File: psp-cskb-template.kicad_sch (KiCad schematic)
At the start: 6 parts, among them J1 Conn_02x26_Odd_Even, J2 Conn_02x26_Odd_Even

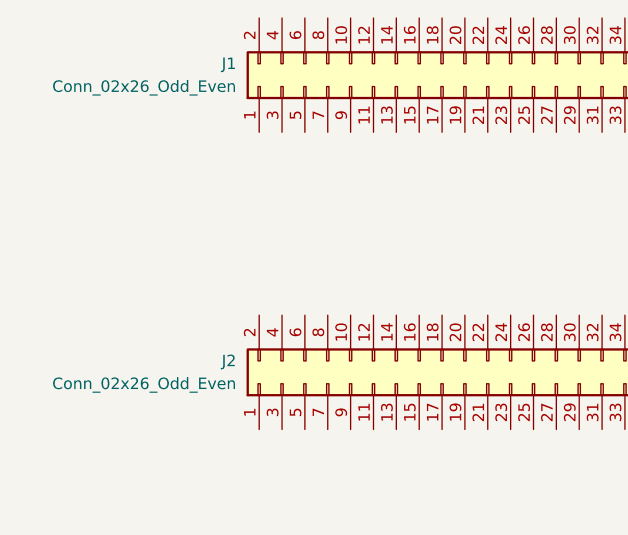
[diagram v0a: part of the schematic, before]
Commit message: flip CSKB header numbers
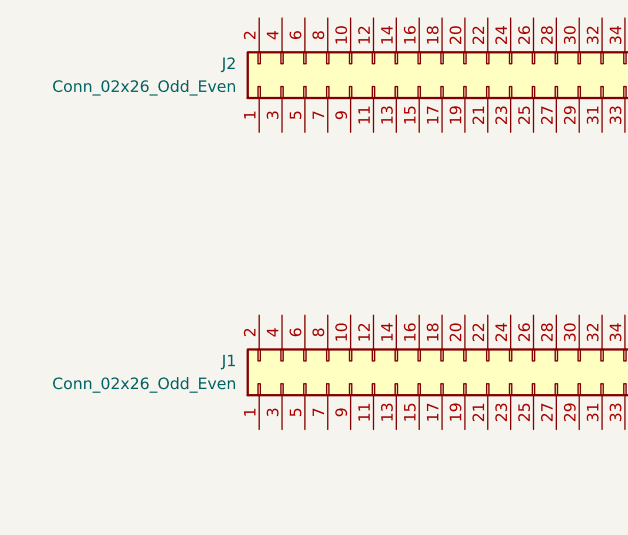
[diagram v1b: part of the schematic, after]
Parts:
- renumbered J2 to J1, J1 to J2
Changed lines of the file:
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@@
 		(dnp no)
 		(fields_autoplaced yes)
-		(property "Reference" "J2"
+		(property "Reference" "J1"
 			(at 422.91 90.1699 90)
 			(effects
@@
 			(project "pspsp_obc"
 				(path "/ceb41114-7a96-4bf5-a24a-5da0a72a9412"
-					(reference "J2")
+					(reference "J1")
 					(unit 1)
 				)
@@
 		(dnp no)
 		(fields_autoplaced yes)
-		(property "Reference" "J1"
+		(property "Reference" "J2"
 			(at 422.91 57.1499 90)
 			(effects
@@
 			(project ""
 				(path "/ceb41114-7a96-4bf5-a24a-5da0a72a9412"
-					(reference "J1")
+					(reference "J2")
 					(unit 1)
 				)
